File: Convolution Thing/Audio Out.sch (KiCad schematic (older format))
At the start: 93 parts

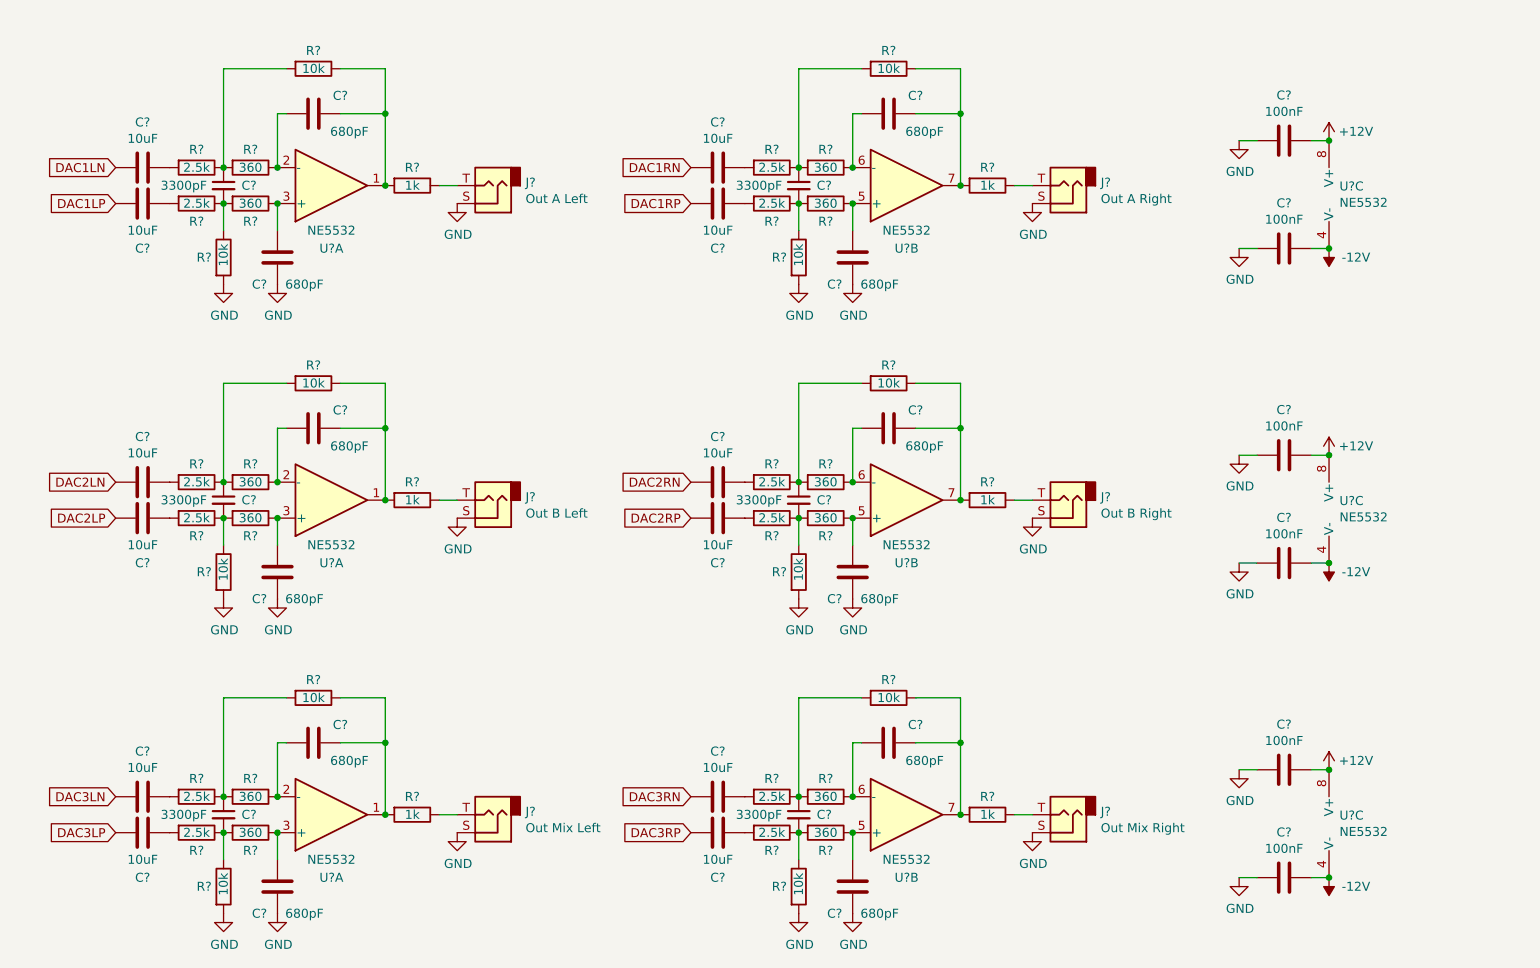
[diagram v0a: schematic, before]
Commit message: New stereo codec and related changes. RIP multi-channel audio.
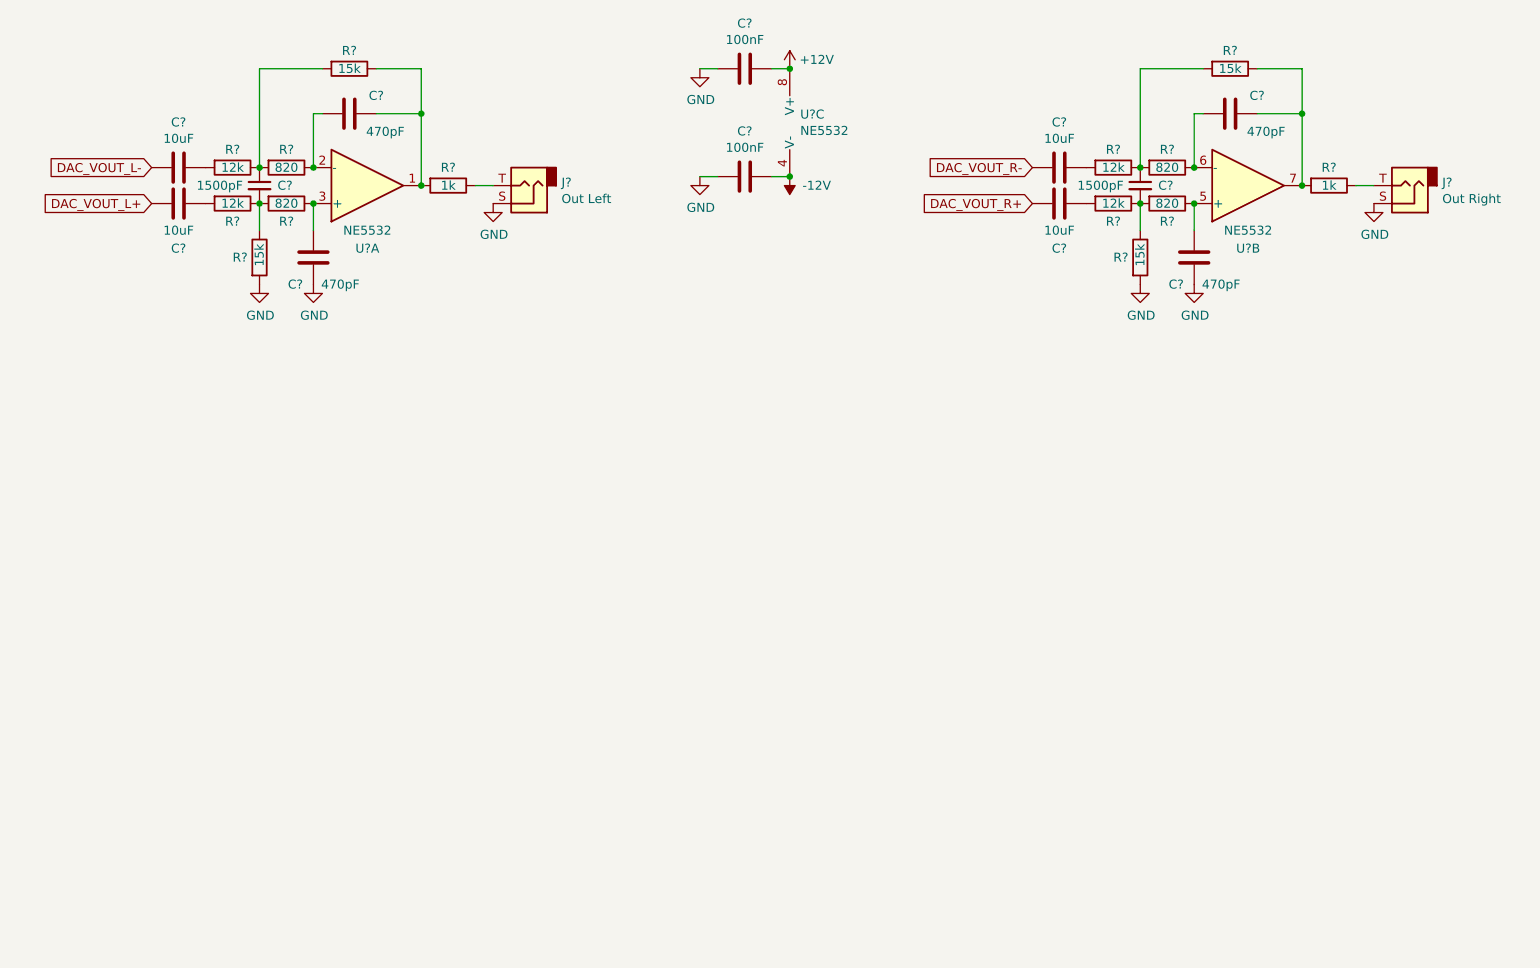
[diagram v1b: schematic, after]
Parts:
- removed C? (x10): 10uF, symbol Device:C
- removed C? (x10): 680pF, symbol Device:C
- removed C? (x5): 3300pF, symbol Device:C_Small
- removed C? (x4): 100nF, symbol Device:C
- removed J?: Out A Right, symbol Connector:AudioJack2
- removed J?: Out B Left, symbol Connector:AudioJack2
- removed J?: Out B Right, symbol Connector:AudioJack2
- removed J?: Out Mix Left, symbol Connector:AudioJack2
- removed J?: Out Mix Right, symbol Connector:AudioJack2
- removed R? (x10): 2.5k, symbol Device:R
- removed R? (x10): 10k, symbol Device:R
- removed R? (x10): 360, symbol Device:R
- removed R? (x5): 1k, symbol Device:R
- removed U? (x7): NE5532, symbol Amplifier_Operational:NE5532
- added C? (x2): 10uF, symbol Device:C
- added C? (x2): 470pF, symbol Device:C
- added C?: 1500pF, symbol Device:C_Small
- added J?: Out Right, symbol Connector:AudioJack2
- added R? (x2): 12k, symbol Device:R
- added R? (x2): 15k, symbol Device:R
- added R? (x2): 820, symbol Device:R
- added R?: 1k, symbol Device:R
- added U?: NE5532, symbol Amplifier_Operational:NE5532
- C? (x2): value 680pF -> 470pF
- C?: value 3300pF -> 1500pF
- J?: value Out A Left -> Out Left
- R? (x2): value 2.5k -> 12k
- R? (x2): value 10k -> 15k
- R? (x2): value 360 -> 820
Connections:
- net GND: now also C?.1, J?.S, R?.2
- net DAC1LN renamed DAC_VOUT_L-
- net DAC1LP renamed DAC_VOUT_L+
- new net: C?.1, R?.2 (x2)
- new net: C?.2, R?.1, U?.5 (+)
- new net: C?.2, R?.1, U?.6 (-)
- new net: C?.1, R?.1, R?.2, U?.7
- new net: C?.1, R?.1, R?.2, R?.2
- new net: C?.2, R?.1, R?.1, R?.2
- new net: J?.T, R?.1
- new net DAC_VOUT_R+: C?.2
- new net DAC_VOUT_R-: C?.2
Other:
- moved on the sheet: C?, J?, R?, U?A, U?C

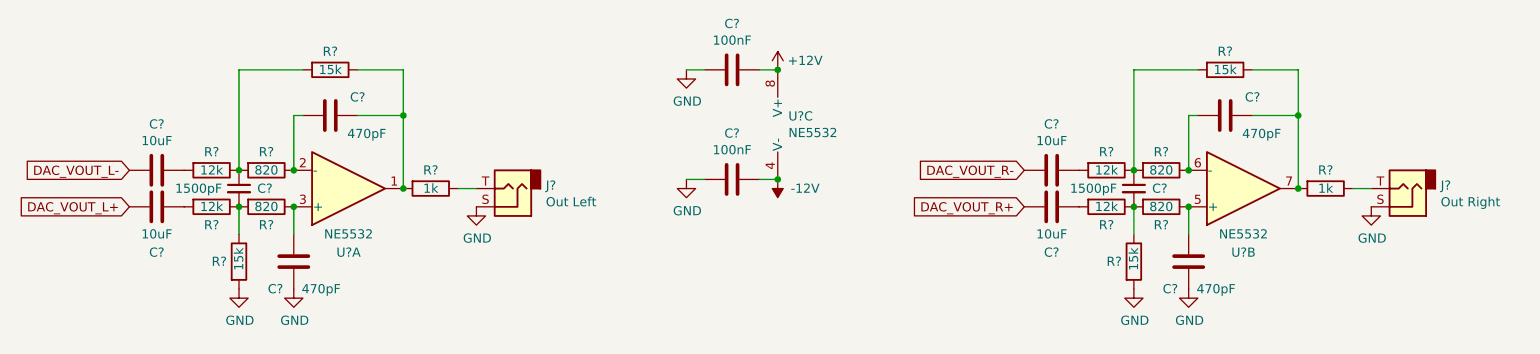
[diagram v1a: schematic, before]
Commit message: Audio I/O, CV input, GPIO work & misc changes
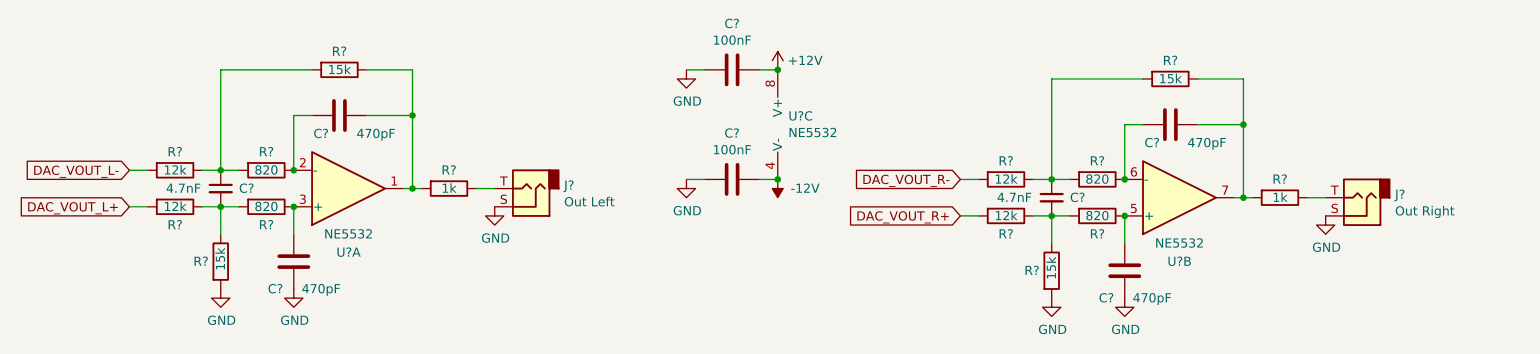
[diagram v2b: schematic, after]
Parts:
- removed C? (x4): 10uF, symbol Device:C
- removed C? (x2): 470pF, symbol Device:C
- removed C?: 1500pF, symbol Device:C_Small
- removed J?: Out Right, symbol Connector:AudioJack2
- removed R? (x2): 12k, symbol Device:R
- removed R? (x2): 15k, symbol Device:R
- removed R? (x2): 820, symbol Device:R
- removed R?: 1k, symbol Device:R
- removed U?: NE5532, symbol Amplifier_Operational:NE5532
- added C?: 4.7nF, symbol Device:C_Small
- added C? (x2): 470pF, symbol Device:C
- added J?: Out Right, symbol Connector:AudioJack2
- added R? (x2): 820, symbol Device:R
- added R?: 1k, symbol Device:R
- added R? (x2): 15k, symbol Device:R
- added R? (x2): 12k, symbol Device:R
- added U?: NE5532, symbol Amplifier_Operational:NE5532
- C?: value 1500pF -> 4.7nF
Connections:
- net DAC_VOUT_L+: now also R?.2
- net DAC_VOUT_L-: now also R?.2
- net DAC_VOUT_R+: now also R?.2
- net DAC_VOUT_R-: now also R?.2
- net GND: now also C?.1, J?.S, R?.2
- new net: C?.2, R?.1, U?.5 (+)
- new net: C?.2, R?.1, U?.6 (-)
- new net: C?.1, R?.1, R?.2, U?.7
- new net: C?.1, R?.1, R?.2, R?.2
- new net: C?.2, R?.1, R?.1, R?.2
- new net: J?.T, R?.1
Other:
- moved on the sheet: C?, J?, R?

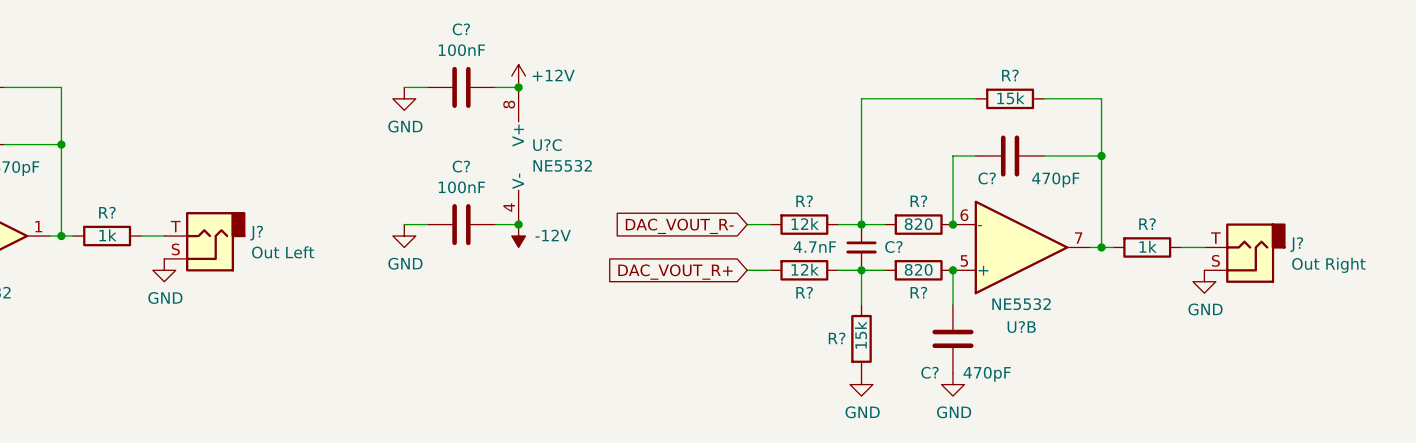
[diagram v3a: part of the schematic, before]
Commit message: Added gate inputs and CM4 / display sockets, made CV inputs 100k, lots of smaller changes. First iteration of schematic now done.
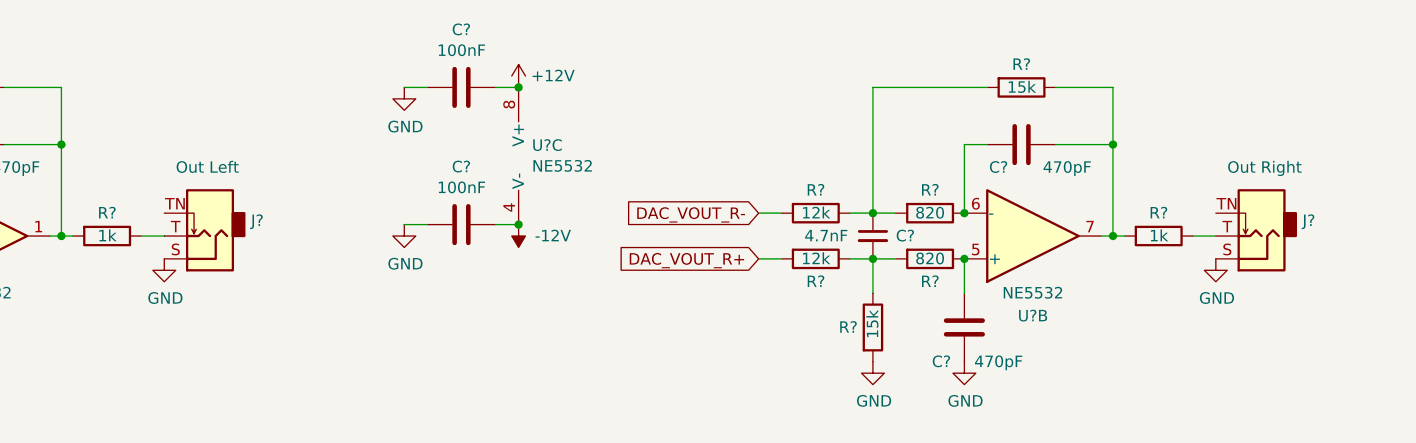
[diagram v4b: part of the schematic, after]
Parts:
- removed J?: Out Right, symbol Connector:AudioJack2
- removed J?: Out Left, symbol Connector:AudioJack2
- added J?: Out Left, symbol Connector:AudioJack2_SwitchT
- added J?: Out Right, symbol Connector:AudioJack2_SwitchT
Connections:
- net GND: now also J?.S, J?.S
- net at R?.1: now also J?.T (x2)
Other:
- moved on the sheet: C?, R?, U?B
